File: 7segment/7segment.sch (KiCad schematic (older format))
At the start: 31 parts, among them J1 AVR-ISP-6, J2 Conn_01x10, J3 Conn_01x02, J4 Conn_01x02, Q1 Q_NPN_BEC, Q2 Q_NPN_BEC, U1 ATmega168PA-AU, U2 HDSP-523

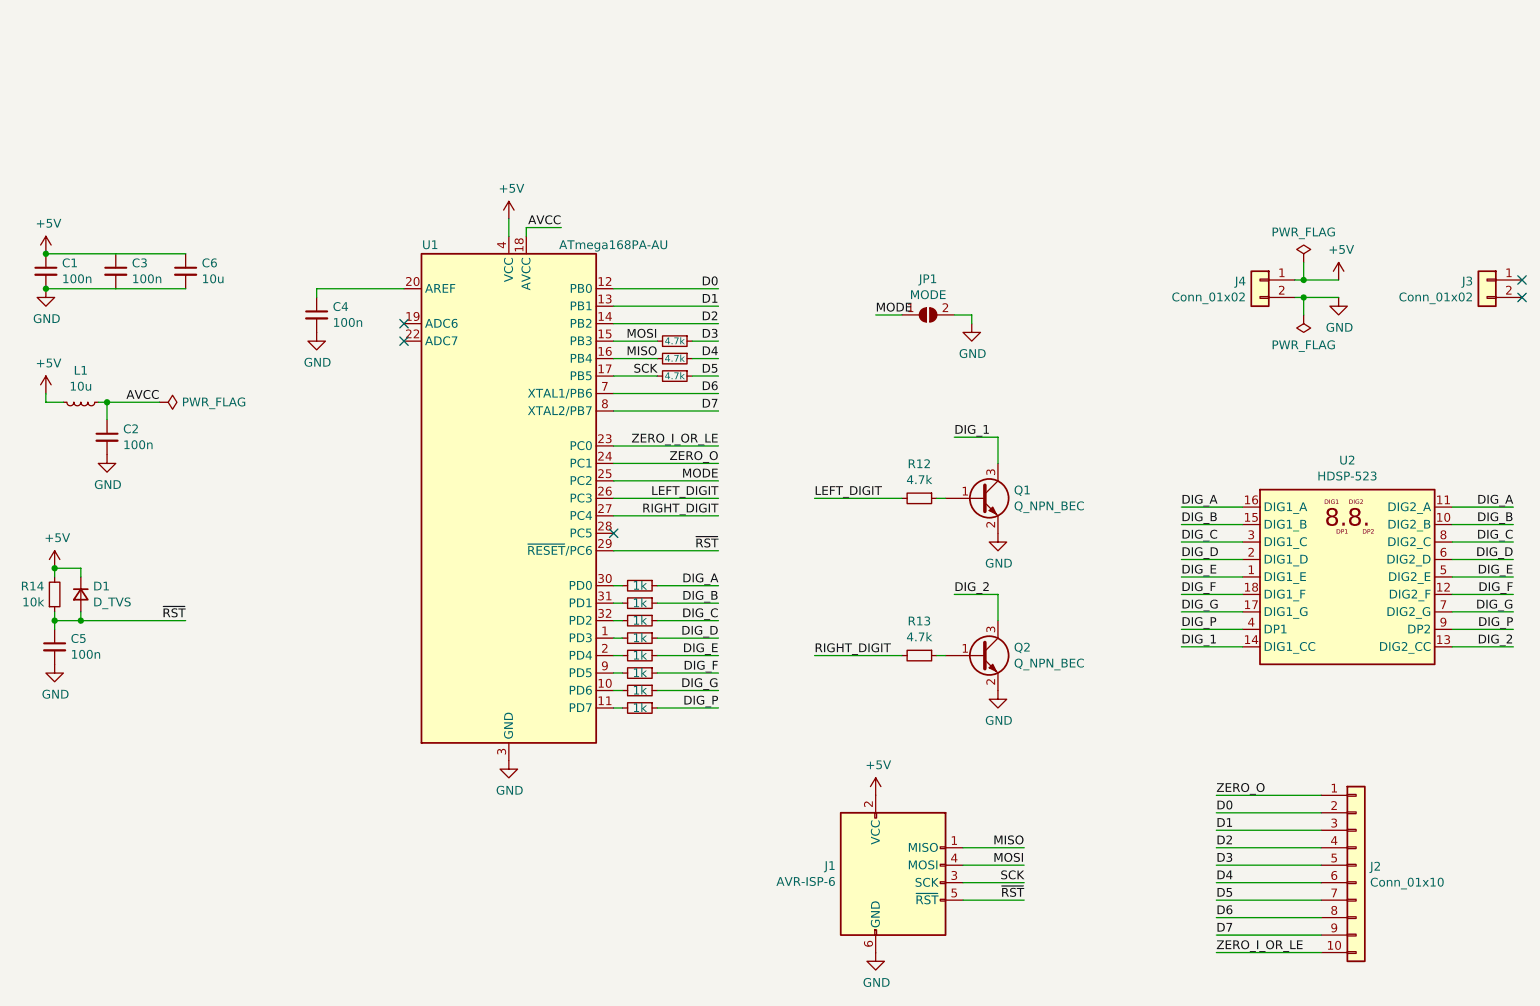
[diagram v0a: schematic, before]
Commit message: Update 7segment
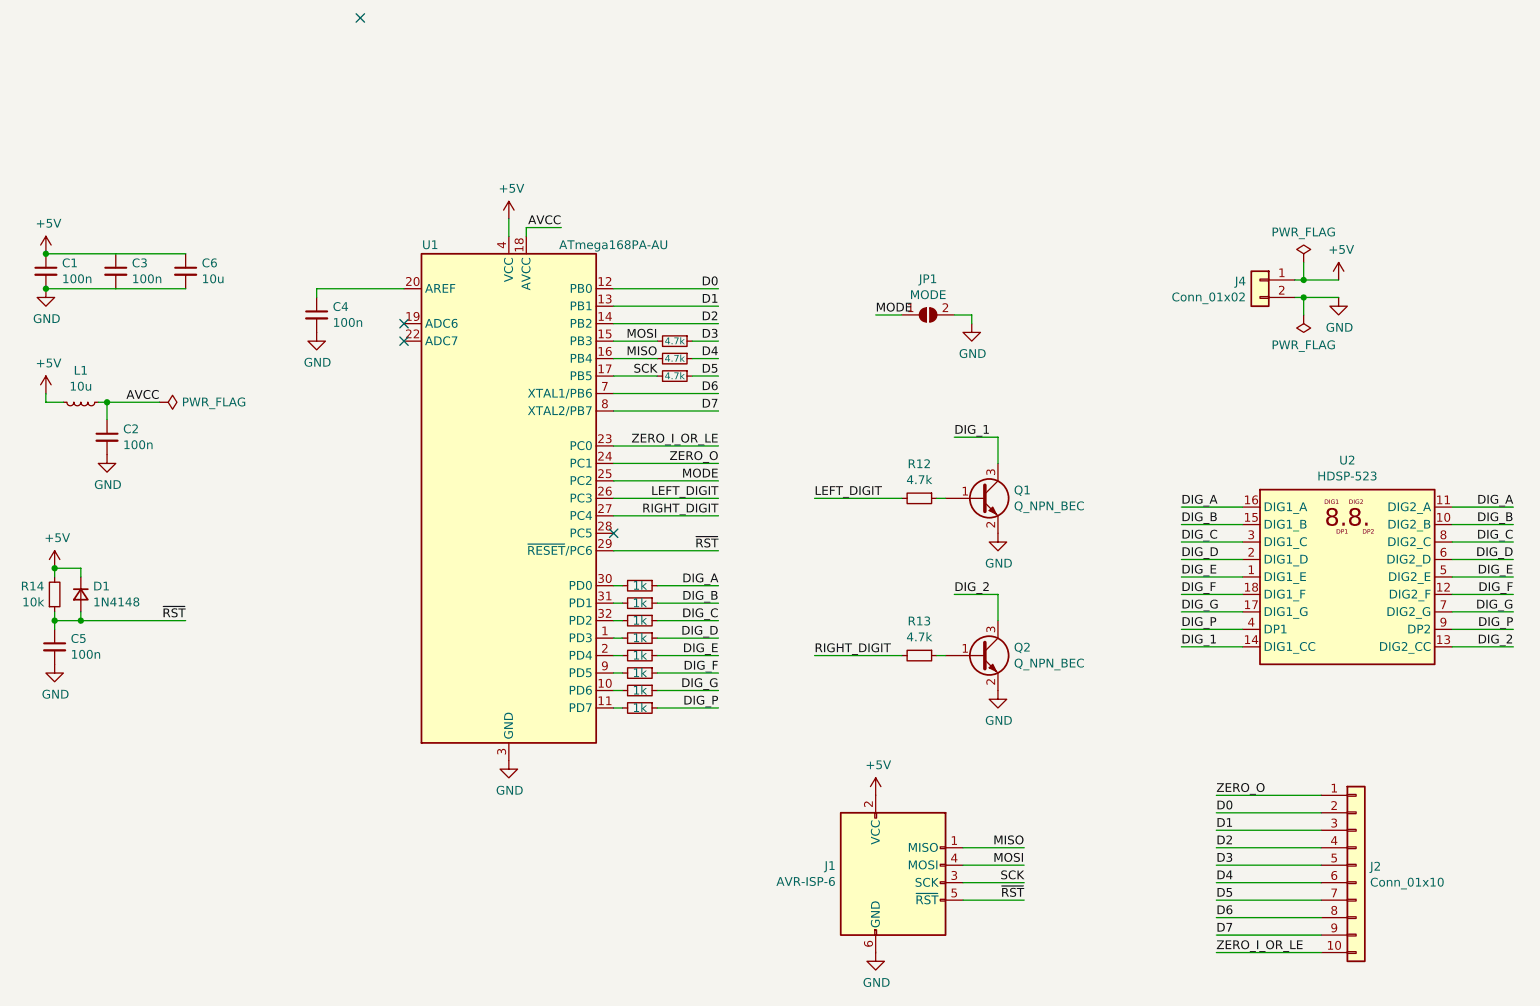
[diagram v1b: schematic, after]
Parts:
- removed J3: Conn_01x02, Connector_PinHeader_2.54mm:PinHeader_1x02_P2.54mm_Vertical_SMD_Pin1Left, symbol Connector_Generic:Conn_01x02
- D1: value D_TVS -> 1N4148; footprint Diode_SMD:D_0402_1005Metric -> Diode_SMD:D_SOD-323F
- L1: footprint Inductor_SMD:L_0402_1005Metric -> Inductor_SMD:L_0603_1608Metric
- R1, R2, R3, R4, R5, R6, R7, R8: footprint Resistor_SMD:R_0402_1005Metric -> Resistor_SMD:R_1206_3216Metric_Pad1.30x1.75mm_HandSolder
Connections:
- no-connect marks 5 -> 4
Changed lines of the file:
@@
-$EndComp
-$Comp
-L Connector_Generic:Conn_01x02 J3
-U 1 1 61BA15BD
-P 9150 1150
-F 0 "J3" H 9230 1142 50  0000 L CNN
-F 1 "Conn_01x02" H 9230 1051 50  0000 L CNN
-F 2 "Connector_PinHeader_2.54mm:PinHeader_1x02_P2.54mm_Vertical_SMD_Pin1Left" H 9150 1150 50  0001 C CNN
-F 3 "~" H 9150 1150 50  0001 C CNN
-	1    9150 1150
-	-1   0    0    -1
 $EndComp
 $Comp
@@
 F 0 "R2" V 4104 3000 50  0001 C CNN
 F 1 "1k" V 4300 3000 50  0000 C CNN
-F 2 "Resistor_SMD:R_0402_1005Metric" H 4300 3000 50  0001 C CNN
+F 2 "Resistor_SMD:R_1206_3216Metric_Pad1.30x1.75mm_HandSolder" H 4300 3000 50  0001 C CNN
 F 3 "~" H 4300 3000 50  0001 C CNN
 	1    4300 3000
@@
 F 0 "R3" V 4104 3100 50  0001 C CNN
 F 1 "1k" V 4300 3100 50  0000 C CNN
-F 2 "Resistor_SMD:R_0402_1005Metric" H 4300 3100 50  0001 C CNN
+F 2 "Resistor_SMD:R_1206_3216Metric_Pad1.30x1.75mm_HandSolder" H 4300 3100 50  0001 C CNN
 F 3 "~" H 4300 3100 50  0001 C CNN
 	1    4300 3100
@@
 F 0 "R4" V 4104 3200 50  0001 C CNN
 F 1 "1k" V 4300 3200 50  0000 C CNN
-F 2 "Resistor_SMD:R_0402_1005Metric" H 4300 3200 50  0001 C CNN
+F 2 "Resistor_SMD:R_1206_3216Metric_Pad1.30x1.75mm_HandSolder" H 4300 3200 50  0001 C CNN
 F 3 "~" H 4300 3200 50  0001 C CNN
 	1    4300 3200
@@
 F 0 "R5" V 4104 3300 50  0001 C CNN
 F 1 "1k" V 4300 3300 50  0000 C CNN
-F 2 "Resistor_SMD:R_0402_1005Metric" H 4300 3300 50  0001 C CNN
+F 2 "Resistor_SMD:R_1206_3216Metric_Pad1.30x1.75mm_HandSolder" H 4300 3300 50  0001 C CNN
 F 3 "~" H 4300 3300 50  0001 C CNN
 	1    4300 3300
@@
 F 0 "R6" V 4104 3400 50  0001 C CNN
 F 1 "1k" V 4300 3400 50  0000 C CNN
-F 2 "Resistor_SMD:R_0402_1005Metric" H 4300 3400 50  0001 C CNN
+F 2 "Resistor_SMD:R_1206_3216Metric_Pad1.30x1.75mm_HandSolder" H 4300 3400 50  0001 C CNN
 F 3 "~" H 4300 3400 50  0001 C CNN
 	1    4300 3400
@@
 F 0 "R7" V 4104 3500 50  0001 C CNN
 F 1 "1k" V 4300 3500 50  0000 C CNN
-F 2 "Resistor_SMD:R_0402_1005Metric" H 4300 3500 50  0001 C CNN
+F 2 "Resistor_SMD:R_1206_3216Metric_Pad1.30x1.75mm_HandSolder" H 4300 3500 50  0001 C CNN
 F 3 "~" H 4300 3500 50  0001 C CNN
 	1    4300 3500
@@
 F 0 "R1" V 4104 2900 50  0001 C CNN
 F 1 "1k" V 4300 2900 50  0000 C CNN
-F 2 "Resistor_SMD:R_0402_1005Metric" H 4300 2900 50  0001 C CNN
+F 2 "Resistor_SMD:R_1206_3216Metric_Pad1.30x1.75mm_HandSolder" H 4300 2900 50  0001 C CNN
 F 3 "~" H 4300 2900 50  0001 C CNN
 	1    4300 2900
@@
 F 0 "R8" V 4104 3600 50  0001 C CNN
 F 1 "1k" V 4300 3600 50  0000 C CNN
-F 2 "Resistor_SMD:R_0402_1005Metric" H 4300 3600 50  0001 C CNN
+F 2 "Resistor_SMD:R_1206_3216Metric_Pad1.30x1.75mm_HandSolder" H 4300 3600 50  0001 C CNN
 F 3 "~" H 4300 3600 50  0001 C CNN
 	1    4300 3600
@@
 F 0 "L1" V 919 1850 50  0000 C CNN
 F 1 "10u" V 1010 1850 50  0000 C CNN
-F 2 "Inductor_SMD:L_0402_1005Metric" H 1100 1850 50  0001 C CNN
+F 2 "Inductor_SMD:L_0603_1608Metric" H 1100 1850 50  0001 C CNN
 F 3 "~" H 1100 1850 50  0001 C CNN
 	1    1100 1850
@@
 P 1100 2950
 F 0 "D1" V 1054 3020 50  0000 L CNN
-F 1 "D_TVS" V 1145 3020 50  0000 L CNN
-F 2 "Diode_SMD:D_0402_1005Metric" V 1100 2950 50  0001 C CNN
+F 1 "1N4148" V 1145 3020 50  0000 L CNN
+F 2 "Diode_SMD:D_SOD-323F" V 1100 2950 50  0001 C CNN
 F 3 "~" V 1100 2950 50  0001 C CNN
 	1    1100 2950
@@
 	1    0    0    -1
 $EndComp
-NoConn ~ 9350 1250
-NoConn ~ 9350 1150
+NoConn ~ 2700 -350
 $EndSCHEMATC
